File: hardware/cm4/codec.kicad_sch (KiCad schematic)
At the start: 14 parts, among them U2 WM8731SEDS, U4 AP2112K-3.3, Y1 12.288MHz

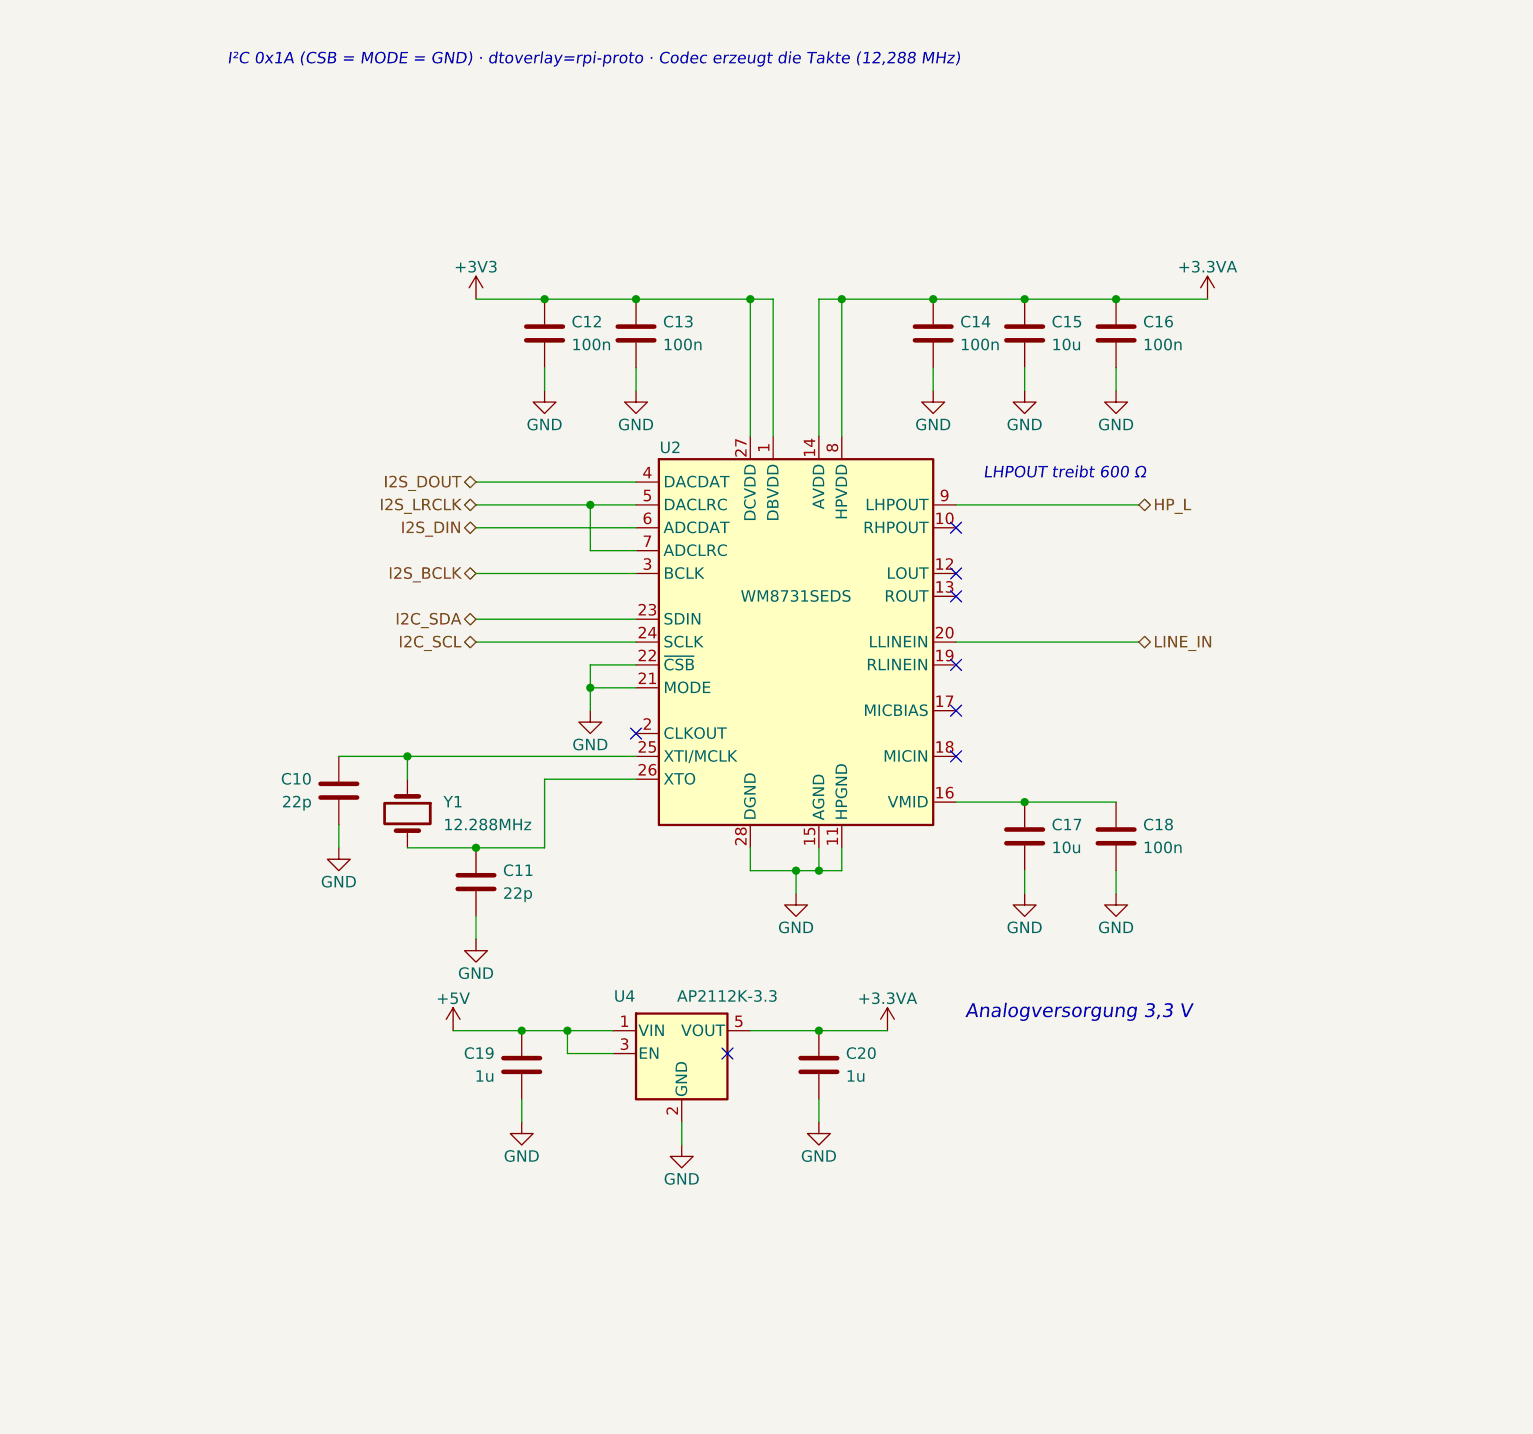
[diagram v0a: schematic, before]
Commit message: CM4-Träger 0.3: Leiterplatte (4 Lagen, JLCPCB), Ein/Aus-Taster, Lüfter, lieferbare Teile
Schaltplan
- Codec TI TLV320AIC3204 statt WM8731 (abgekündigt); MCLK 12 MHz, Reset GPIO26, I²C an GPIO0/1
- Ein/Aus-Taster an GPIO3 (gpio-shutdown im Betrieb, Bootloader-Wecken im Halt)
- Lüfterblatt: AO3400A an GPIO12, Freilaufdiode, JST-PH-Anschluss; gpio-fan über SoC-Temperatur
- Konfig-Taster SW2 und Status-LED D3; Würth RJ45/RJ12, Bourns SM-LP-5001, TPD4E05U06
- reproduzierbare UUIDs (Schaltplan ↔ Platine bleiben verknüpft), eigene Footprints in hardware/bibliothek

Leiterplatte (erzeuge_layout.py)
- 110 × 85 mm, F.Cu / In1 GND / In2 +3V3 / B.Cu, JLC04161H-7628, JLCPCB-Regeln (.kicad_dru)
- CM4-Lage nach CM4IO-Referenz, Antennen-Sperrzone, isolierte Bereiche GND_ISO/GNDA mit Trennstreifen
- eigenes Fanout zu den Ebenen, Routing mit FreeRouting 1.9.0 über xvfb (2.x: Telemetrie an)
- DRC ohne Verstöße, 0 offene Verbindungen, Schaltplan ↔ Platine identisch
- Bestellliste für Digikey mit geprüftem Lagerbestand
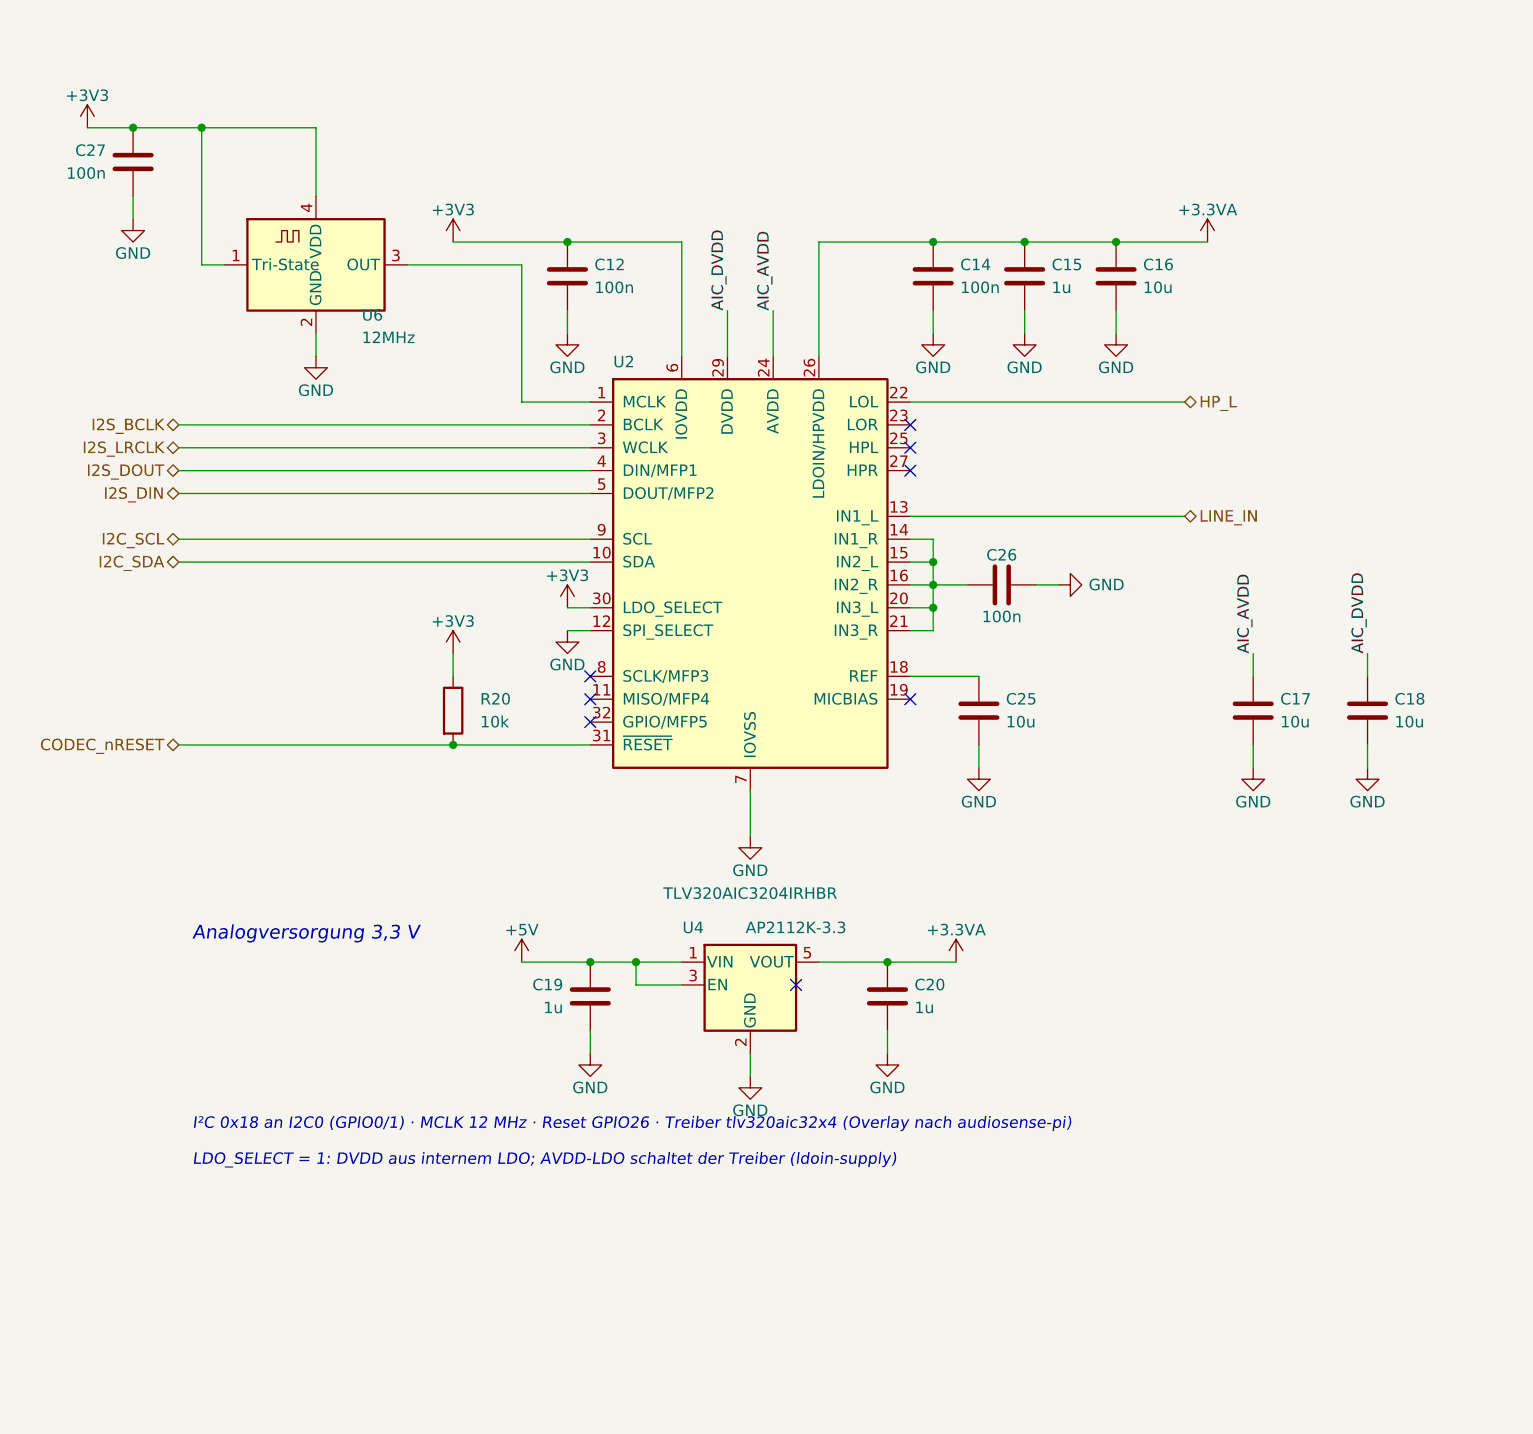
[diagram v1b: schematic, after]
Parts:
- removed C10, C11: 22p, Capacitor_SMD:C_0603_1608Metric, symbol Device:C
- removed C13: 100n, Capacitor_SMD:C_0603_1608Metric, symbol Device:C
- removed U2: WM8731SEDS, Package_SO:SSOP-28_5.3x10.2mm_P0.65mm, symbol Audio:WM8731SEDS
- removed Y1: 12.288MHz, Crystal:Crystal_SMD_HC49-SD, symbol Device:Crystal
- added C25: 10u, Capacitor_SMD:C_0805_2012Metric, symbol Device:C
- added C26, C27: 100n, Capacitor_SMD:C_0603_1608Metric, symbol Device:C
- added R20: 10k, Resistor_SMD:R_0603_1608Metric, symbol Device:R
- added U2: TLV320AIC3204IRHBR, Package_DFN_QFN:Texas_RHB0032E_VQFN-32-1EP_5x5mm_P0.5mm_EP3.45x3.45mm_ThermalVias, symbol Sopho2SIP:TLV320AIC3204
- added U6: 12MHz, Oscillator:Oscillator_SMD_ECS_2520MV-xxx-xx-4Pin_2.5x2.0mm, symbol Oscillator:ECS-2520MV-xxx-xx
- C15: value 10u -> 1u; footprint Capacitor_SMD:C_0805_2012Metric -> Capacitor_SMD:C_0603_1608Metric
- C16, C18: value 100n -> 10u; footprint Capacitor_SMD:C_0603_1608Metric -> Capacitor_SMD:C_0805_2012Metric
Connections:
- net +3.3VA: now also U2.26 (LDOIN/HPVDD)
- net +3V3: now also C27.1, R20.1, U2.30 (LDO_SELECT), U2.6 (IOVDD), U6.1 (Tri-State), U6.4 (VDD)
- net GND: now also C25.2, C26.2, C27.2, U2.12 (SPI_SELECT), U2.17 (AVSS), U2.28 (DVSS), U2.33 (EP), U2.7 (IOVSS), U6.2 (GND)
- net HP_L: now also U2.22 (LOL)
- net I2C_SCL: now also U2.9 (SCL)
- net I2C_SDA: now also U2.10 (SDA)
- net I2S_BCLK: now also U2.2 (BCLK)
- net I2S_DIN: now also U2.5 (DOUT/MFP2)
- net I2S_DOUT: now also U2.4 (DIN/MFP1)
- net I2S_LRCLK: now also U2.3 (WCLK)
- net LINE_IN: now also U2.13 (IN1_L)
- net AIC_AVDD: now reaches C17.1
- net AIC_AVDD: now also U2.24 (AVDD); no longer C18.1
- new net: C25.1, U2.18 (REF)
- new net: U2.1 (MCLK), U6.3 (OUT)
- new net: C26.1, U2.14 (IN1_R), U2.15 (IN2_L), U2.16 (IN2_R), U2.20 (IN3_L), U2.21 (IN3_R)
- new net AIC_DVDD: C18.1, U2.29 (DVDD)
- new net CODEC_nRESET: R20.2, U2.31 (~{RESET})
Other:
- note added: "I²C 0x18 an I2C0 (GPIO0/1) · MCLK 12 MHz · Reset GPIO26 · Treiber tlv320aic32x4 (Overlay nach audiosense-pi)"
- note added: "LDO_SELECT = 1: DVDD aus internem LDO; AVDD-LDO schaltet der Treiber (ldoin-supply)"
- note removed: "I²C 0x1A (CSB = MODE = GND) · dtoverlay=rpi-proto · Codec erzeugt die Takte (12,288 MHz)"
- note removed: "LHPOUT treibt 600 Ω"
- title: Audio-Codec WM8731 -> Audio-Codec TLV320AIC3204

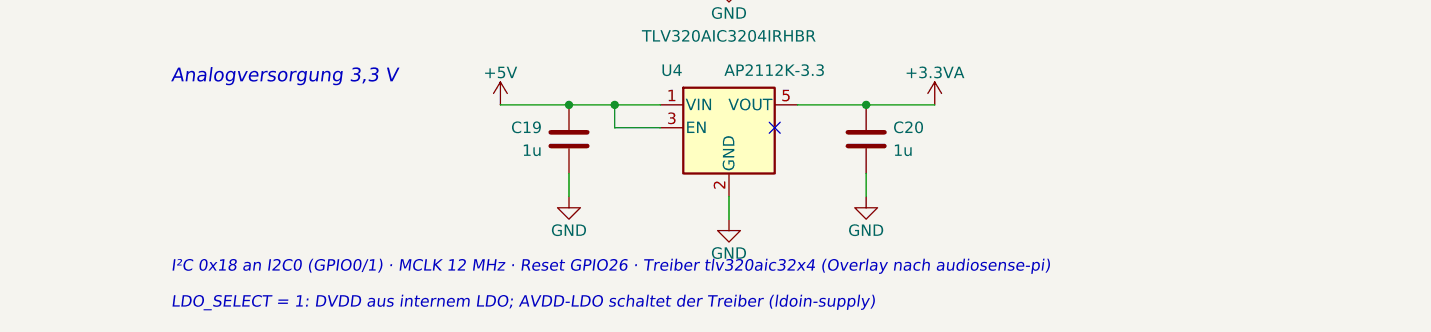
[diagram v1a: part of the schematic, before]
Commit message: Schaltplan: Hinweise als Textkästen (KiCad bricht um); Texte werden in den Generator zurückgeführt
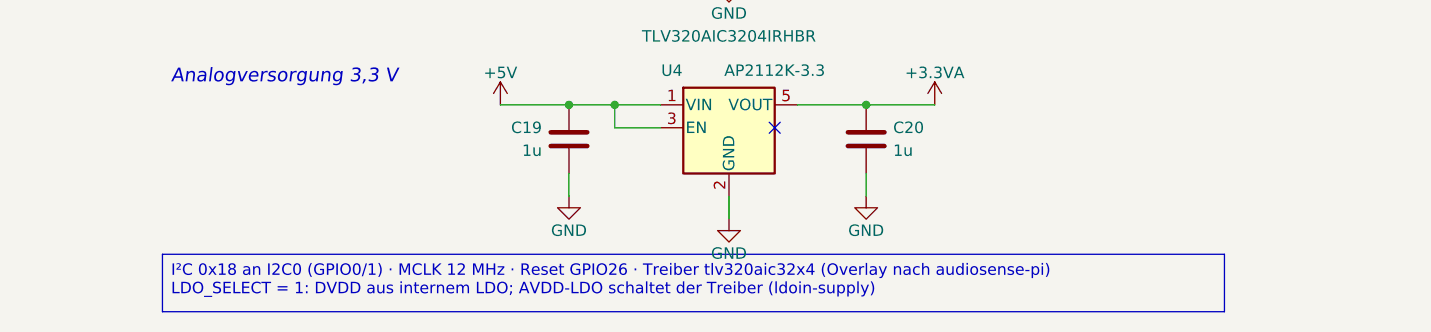
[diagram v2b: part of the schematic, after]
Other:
- note removed: "I²C 0x18 an I2C0 (GPIO0/1) · MCLK 12 MHz · Reset GPIO26 · Treiber tlv320aic32x4 (Overlay nach audiosense-pi)"
- note removed: "LDO_SELECT = 1: DVDD aus internem LDO; AVDD-LDO schaltet der Treiber (ldoin-supply)"
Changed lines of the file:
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@@
 	(label "AIC_AVDD" (at 267.97 134.62 90) (effects (font (size 1.27 1.27)) (justify left bottom)))
 	(label "AIC_DVDD" (at 280.67 134.62 90) (effects (font (size 1.27 1.27)) (justify left bottom)))
-	(text "I²C 0x18 an I2C0 (GPIO0/1) · MCLK 12 MHz · Reset GPIO26 · Treiber tlv320aic32x4 (Overlay nach audiosense-pi)" (exclude_from_sim no) (at 150.09 187.73 0) (effects (font (size 1.27 1.27) italic) (justify left bottom)))
-	(text "LDO_SELECT = 1: DVDD aus internem LDO; AVDD-LDO schaltet der Treiber (ldoin-supply)" (exclude_from_sim no) (at 150.09 191.73 0) (effects (font (size 1.27 1.27) italic) (justify left bottom)))
 	(text "Analogversorgung 3,3 V" (exclude_from_sim no) (at 150.09 166.73 0) (effects (font (size 1.524 1.524) italic) (justify left bottom)))
+	(text_box "I²C 0x18 an I2C0 (GPIO0/1) · MCLK 12 MHz · Reset GPIO26 · Treiber tlv320aic32x4 (Overlay nach audiosense-pi)\nLDO_SELECT = 1: DVDD aus internem LDO; AVDD-LDO schaltet der Treiber (ldoin-supply)" (exclude_from_sim no) (at 149.14 185.51 0) (size 118 6.38) (margins 0.9525 0.9525 0.9525 0.9525) (stroke (width 0.1) (type solid) (color 132 132 132 1)) (fill (type color) (color 255 255 230 1)) (effects (font (size 1.27 1.27)) (justify left top)))
 	(embedded_fonts no)
 )

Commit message: CM4-Schaltplan: Handänderungen übernommen (Handlage für 8 Blätter, 2 Texte zurückgeführt); Kastenhöhen aus gemessenen Zeichenbreiten
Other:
- moved on the sheet: C12, C14, C15, C16, C17, C18, C19, C20, R20, U4
